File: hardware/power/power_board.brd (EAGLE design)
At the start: 75 x 64.5 mm, 6 parts, among them J1 FASTON_MALE_RA_BLADE, J2 FASTON_MALE_RA_BLADE, J3 12v, J4 5v, U1 PDQ30-Q24-S5-D, U2 PDQ30-Q24-S12-D

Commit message: Power updates
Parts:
- added J5, J6, J7, J8: XT30PW-F, timlib:XT30PW-F
- added R1: 100, rcl:R0603
- added U$10, U$9: 2, timlib:PWR163
- added U$11: PSMN1R0-40YSH, timlib:LFPAK56E
- moved J3 107.3 mm to (85.2, 81.6), turned to 90 degrees
- moved J4 94.3 mm to (85.2, 71.0), turned to 90 degrees
- moved U2 74.8 mm to (15.8, 77.0), turned to 0 degrees
- moved U1 45.6 mm to (15.8, 50.9), turned to 180 degrees
- moved J1 42.5 mm to (50.0, 57.3), turned to 180 degrees
- moved J2 23.8 mm to (50.0, 34.7), turned to 180 degrees
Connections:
- new net N$1: U$10.P$1, U$11.5
- net +24V: now also J5.P$2, J6.P$2, J7.P$2, J8.P$2
- net GND: now also J5.P$1, J6.P$1, J7.P$1, J8.P$1, U$11.1, U$11.2, U$11.3
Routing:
- removed copper zone on layer 16, net GND_5V
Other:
- board size 75 x 64.5 mm -> 92 x 92 mm

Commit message: Power board updates
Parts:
- added R2, R5: 2, timlib:PWR163
- added R4: 100, rcl:R0603
- added U$12: SMAJ12A, timlib:DO-214AC
- U$10: value 2 -> SMAJ12A; device timlib:PWR163 -> timlib:DO-214AC
- U$9: value 2 -> PSMN1R0-40YSH; device timlib:PWR163 -> timlib:LFPAK56E
- moved U$11 40.8 mm to (24.3, 33.9), turned to 270 degrees
- moved U$10 40.6 mm to (23.6, 16.5)
- moved R1 37.9 mm to (23.2, 24.0)
- moved U$9 8.64 mm to (15.6, 16.8), turned to 90 degrees
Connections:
- new net N$2: R1.1, U$11.4, U$12.C
- new net N$3: R5.P$2, U$9.5
- new net N$4: R4.1, U$10.C, U$9.4
- net GND: now also U$10.A, U$12.A, U$9.1, U$9.2, U$9.3
- net N$1: now also R2.P$2; no longer U$10.P$1
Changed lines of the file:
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@@
 <element name="U1" library="timlib" library_urn="urn:adsk.eagle:library:16152524" package="PDQ30-D" package3d_urn="urn:adsk.eagle:package:16187995/2" value="PDQ30-Q24-S5-D" x="15.75" y="50.85" smashed="yes" rot="R180"/>
 <element name="U2" library="timlib" library_urn="urn:adsk.eagle:library:16152524" package="PDQ30-D" package3d_urn="urn:adsk.eagle:package:16187995/2" value="PDQ30-Q24-S12-D" x="15.75" y="76.95" smashed="yes"/>
-<element name="J5" library="timlib" library_urn="urn:adsk.eagle:library:16152524" package="XT30PW-F" package3d_urn="urn:adsk.eagle:package:16203166/6" value="XT30PW-F" x="80.85" y="25.75" smashed="yes" rot="R270" grouprefs="EXTERNAL_PLUGS LEG_POWER"/>
-<element name="J6" library="timlib" library_urn="urn:adsk.eagle:library:16152524" package="XT30PW-F" package3d_urn="urn:adsk.eagle:package:16203166/6" value="XT30PW-F" x="80.85" y="39.5" smashed="yes" rot="R270" grouprefs="EXTERNAL_PLUGS LEG_POWER"/>
-<element name="J7" library="timlib" library_urn="urn:adsk.eagle:library:16152524" package="XT30PW-F" package3d_urn="urn:adsk.eagle:package:16203166/6" value="XT30PW-F" x="80.85" y="53.25" smashed="yes" rot="R270" grouprefs="EXTERNAL_PLUGS LEG_POWER"/>
-<element name="J8" library="timlib" library_urn="urn:adsk.eagle:library:16152524" package="XT30PW-F" package3d_urn="urn:adsk.eagle:package:16203166/6" value="XT30PW-F" x="80.85" y="12" smashed="yes" rot="R270" grouprefs="EXTERNAL_PLUGS LEG_POWER"/>
-<element name="U$9" library="timlib" library_urn="urn:adsk.eagle:library:16152524" package="PWR163" package3d_urn="urn:adsk.eagle:package:16220013/7" value="2" x="8.85" y="22.2" smashed="yes" rot="R180"/>
-<element name="U$10" library="timlib" library_urn="urn:adsk.eagle:library:16152524" package="PWR163" package3d_urn="urn:adsk.eagle:package:16220013/7" value="2" x="34.2" y="55.65" smashed="yes" rot="R270"/>
-<element name="U$11" library="timlib" library_urn="urn:adsk.eagle:library:16152524" package="LFPAK56E" package3d_urn="urn:adsk.eagle:package:16249927/3" value="PSMN1R0-40YSH" x="-2.7" y="3.3" smashed="yes"/>
-<element name="R1" library="rcl" library_urn="urn:adsk.eagle:library:334" package="R0603" package3d_urn="urn:adsk.eagle:package:23555/3" value="100" x="-3.6" y="-2.7" smashed="yes">
-<attribute name="NAME" x="-4.235" y="-2.065" size="1.27" layer="25"/>
-<attribute name="POPULARITY" value="77" x="-3.6" y="-2.7" size="1.778" layer="27" display="off"/>
-<attribute name="SPICEPREFIX" value="R" x="-3.6" y="-2.7" size="1.778" layer="27" display="off"/>
-<attribute name="VALUE" x="-4.235" y="-4.605" size="1.27" layer="27"/>
+<element name="J5" library="timlib" library_urn="urn:adsk.eagle:library:16152524" package="XT30PW-F" package3d_urn="urn:adsk.eagle:package:16203166/6" value="XT30PW-F" x="80.85" y="25.75" smashed="yes" rot="R270" grouprefs="LEG_POWER EXTERNAL_PLUGS"/>
+<element name="J6" library="timlib" library_urn="urn:adsk.eagle:library:16152524" package="XT30PW-F" package3d_urn="urn:adsk.eagle:package:16203166/6" value="XT30PW-F" x="80.85" y="39.5" smashed="yes" rot="R270" grouprefs="LEG_POWER EXTERNAL_PLUGS"/>
+<element name="J7" library="timlib" library_urn="urn:adsk.eagle:library:16152524" package="XT30PW-F" package3d_urn="urn:adsk.eagle:package:16203166/6" value="XT30PW-F" x="80.85" y="53.25" smashed="yes" rot="R270" grouprefs="LEG_POWER EXTERNAL_PLUGS"/>
+<element name="J8" library="timlib" library_urn="urn:adsk.eagle:library:16152524" package="XT30PW-F" package3d_urn="urn:adsk.eagle:package:16203166/6" value="XT30PW-F" x="80.85" y="12" smashed="yes" rot="R270" grouprefs="LEG_POWER EXTERNAL_PLUGS"/>
+<element name="U$11" library="timlib" library_urn="urn:adsk.eagle:library:16152524" package="LFPAK56E" package3d_urn="urn:adsk.eagle:package:16249927/3" value="PSMN1R0-40YSH" x="24.3" y="33.9" smashed="yes" rot="R270"/>
+<element name="R1" library="rcl" library_urn="urn:adsk.eagle:library:334" package="R0603" package3d_urn="urn:adsk.eagle:package:23555/3" value="100" x="23.25" y="24" smashed="yes">
+<attribute name="NAME" x="22.615" y="24.635" size="1.27" layer="25"/>
+<attribute name="POPULARITY" value="77" x="23.25" y="24" size="1.778" layer="27" display="off"/>
+<attribute name="SPICEPREFIX" value="R" x="23.25" y="24" size="1.778" layer="27" display="off"/>
+<attribute name="VALUE" x="22.615" y="22.095" size="1.27" layer="27"/>
 </element>
+<element name="U$12" library="timlib" library_urn="urn:adsk.eagle:library:16152524" package="DO-214AC" package3d_urn="urn:adsk.eagle:package:16356227/5" value="SMAJ12A" x="33.45" y="25.95" smashed="yes" rot="R90">
+<attribute name="NAME" x="31.545" y="23.41" size="1.27" layer="25" rot="R90"/>
+<attribute name="VALUE" x="36.625" y="23.41" size="1.27" layer="27" rot="R90"/>
+</element>
+<element name="R2" library="timlib" library_urn="urn:adsk.eagle:library:16152524" package="PWR163" package3d_urn="urn:adsk.eagle:package:16220013/7" value="2" x="34.95" y="42.6" smashed="yes" rot="R270"/>
+<element name="U$9" library="timlib" library_urn="urn:adsk.eagle:library:16152524" package="LFPAK56E" package3d_urn="urn:adsk.eagle:package:16249927/3" value="PSMN1R0-40YSH" x="15.6" y="16.8" smashed="yes" rot="R90"/>
+<element name="R4" library="rcl" library_urn="urn:adsk.eagle:library:334" package="R0603" package3d_urn="urn:adsk.eagle:package:23555/3" value="100" x="29.1" y="19.95" smashed="yes">
+<attribute name="NAME" x="28.465" y="20.585" size="1.27" layer="25"/>
+<attribute name="POPULARITY" value="77" x="24" y="41.7" size="1.778" layer="27" display="off"/>
+<attribute name="SPICEPREFIX" value="R" x="24" y="41.7" size="1.778" layer="27" display="off"/>
+<attribute name="VALUE" x="28.465" y="18.045" size="1.27" layer="27"/>
+</element>
+<element name="U$10" library="timlib" library_urn="urn:adsk.eagle:library:16152524" package="DO-214AC" package3d_urn="urn:adsk.eagle:package:16356227/5" value="SMAJ12A" x="23.55" y="16.5" smashed="yes" rot="R270">
+<attribute name="NAME" x="25.455" y="19.04" size="1.27" layer="25" rot="R270"/>
+<attribute name="VALUE" x="20.375" y="19.04" size="1.27" layer="27" rot="R270"/>
+</element>
+<element name="R5" library="timlib" library_urn="urn:adsk.eagle:library:16152524" package="PWR163" package3d_urn="urn:adsk.eagle:package:16220013/7" value="2" x="7.35" y="14.1" smashed="yes" rot="R180"/>
 </elements>
 <signals>
@@
 <contactref element="U$11" pad="1"/>
 <contactref element="U$11" pad="2"/>
+<contactref element="U$12" pad="A"/>
+<contactref element="U$9" pad="1"/>
+<contactref element="U$9" pad="2"/>
+<contactref element="U$9" pad="3"/>
+<contactref element="U$10" pad="A"/>
 <wire x1="75.85" y1="42" x2="75.85" y2="55.75" width="0" layer="19" extent="1-1"/>
 <wire x1="75.85" y1="28.25" x2="75.85" y2="42" width="0" layer="19" extent="1-1"/>
@@
 <wire x1="52.54" y1="34.7" x2="75.85" y2="28.25" width="0" layer="19" extent="1-1"/>
 <wire x1="47.46" y1="34.7" x2="52.54" y2="34.7" width="0" layer="19" extent="1-1"/>
-<wire x1="13.21" y1="40.69" x2="47.46" y2="34.7" width="0" layer="19" extent="1-1"/>
-<wire x1="-2.065" y1="0.575" x2="13.21" y2="40.69" width="0" layer="19" extent="1-1"/>
-<wire x1="-3.335" y1="0.575" x2="-2.065" y2="0.575" width="0" layer="19" extent="1-1"/>
-<wire x1="-4.605" y1="0.575" x2="-3.335" y2="0.575" width="0" layer="19" extent="1-1"/>
+<wire x1="21.575" y1="35.805" x2="47.46" y2="34.7" width="0" layer="19" extent="1-1"/>
+<wire x1="21.575" y1="34.535" x2="21.575" y2="35.805" width="0" layer="19" extent="1-1"/>
+<wire x1="21.575" y1="33.265" x2="21.575" y2="34.535" width="0" layer="19" extent="1-1"/>
+<wire x1="33.45" y1="27.975" x2="21.575" y2="33.265" width="0" layer="19" extent="1-1"/>
+<wire x1="13.21" y1="40.69" x2="21.575" y2="35.805" width="0" layer="19" extent="1-1"/>
 <wire x1="18.29" y1="87.11" x2="13.21" y2="40.69" width="0" layer="19" extent="1-1"/>
+<wire x1="23.55" y1="14.475" x2="33.45" y2="27.975" width="0" layer="19" extent="1-1"/>
+<wire x1="18.325" y1="14.895" x2="23.55" y2="14.475" width="0" layer="19" extent="1-1"/>
+<wire x1="18.325" y1="16.165" x2="18.325" y2="14.895" width="0" layer="19" extent="1-1"/>
+<wire x1="18.325" y1="17.435" x2="18.325" y2="16.165" width="0" layer="19" extent="1-1"/>
 </signal>
 <signal name="N$1">
-<contactref element="U$10" pad="P$1"/>
 <contactref element="U$11" pad="5"/>
-<wire x1="-2.7" y1="5.332" x2="32.295" y2="58.19" width="0" layer="19" extent="1-1"/>
+<contactref element="R2" pad="P$2"/>
+<wire x1="26.332" y1="33.9" x2="33.045" y2="40.06" width="0" layer="19" extent="1-1"/>
+</signal>
+<signal name="N$2">
+<contactref element="U$12" pad="C"/>
+<contactref element="U$11" pad="4"/>
+<contactref element="R1" pad="1"/>
+<wire x1="22.4" y1="24" x2="33.45" y2="23.925" width="0" layer="19" extent="1-1"/>
+<wire x1="21.575" y1="31.995" x2="22.4" y2="24" width="0" layer="19" extent="1-1"/>
+</signal>
+<signal name="N$3">
+<contactref element="U$9" pad="5"/>
+<contactref element="R5" pad="P$2"/>
+<wire x1="13.568" y1="16.8" x2="4.81" y2="16.005" width="0" layer="19" extent="1-1"/>
+</signal>
+<signal name="N$4">
+<contactref element="U$10" pad="C"/>
+<contactref element="U$9" pad="4"/>
+<contactref element="R4" pad="1"/>
+<wire x1="23.55" y1="18.525" x2="28.25" y2="19.95" width="0" layer="19" extent="1-1"/>
+<wire x1="18.325" y1="18.705" x2="23.55" y2="18.525" width="0" layer="19" extent="1-1"/>
 </signal>
 </signals>

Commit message: Missing some caps
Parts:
- added C1, C2, C3, C4, C5, C6, C7: 220uf, timlib:C_ELEC_8X11_5
- added IC1, IC2: LM321MF, linear:SOT23-5
- added R10, R15, R17, R19, R7, R9: 100k\, rcl:R0603
- added R11: 4.7k, rcl:R0603
- added R12: 2, timlib:PWR163
- added R13, R3: 873.1k, rcl:R0603
- added R14: 100k, rcl:R0603
- added R16, R18, R6, R8: 400k, rcl:R0603
- added U$1, U$2, U$3, U$6: PSMN1R0-40YSH, timlib:LFPAK56E
- added U$4, U$7, U$8: SMAJ12A, timlib:DO-214AC
- added U$5: LP2951ACMM/NOPB, timlib:LP2591
- R1: value 100 -> 4.7k
- R4: value 100 -> 100k
- R5: value 2 -> 100k\; device timlib:PWR163 -> rcl:R0603
- U$9: value PSMN1R0-40YSH -> LP2951ACMM/NOPB; device timlib:LFPAK56E -> timlib:LP2591
- moved U$9 48.7 mm to (64.2, 13.5), turned to 0 degrees
- moved R5 47.2 mm to (53.4, 24.3), turned to 0 degrees
- moved U$10 40.9 mm to (3.00, -18.9), turned to 0 degrees
- moved R2 40.4 mm to (7.05, 13.3), turned to 180 degrees
- moved R4 27.4 mm to (54.8, 10.3)
- moved R1 24.3 mm to (39.9, 41.7)
- moved U$12 19.0 mm to (45.1, 41.0), turned to 0 degrees
- moved U$11 11.0 mm to (33.1, 40.4), turned to 90 degrees
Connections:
- net GND_12V renamed -12VOUT
- net GND_5V renamed -5VOUT
- net ISO_+12V renamed +12VOUT
- net ISO_+5V renamed +5VOUT
- removed net +24V: J1.P$1, J1.P$2, J5.P$2, J6.P$2, J7.P$2, J8.P$2, U1.P$1, U2.P$1
- new net BATT_+24V: C1.1, C2.1, C3.1, C4.1, C5.1, C6.1, C7.1, J1.P$1, J1.P$2, J5.P$2, J6.P$2, J7.P$2, J8.P$2, U$5.8, U$9.8, U1.P$1, U2.P$1
- new net BATT_GND: IC1.2, IC2.2, J2.P$1, J2.P$2, R14.1, R16.1, R18.1, R4.1, R6.1, R8.1, U$1.1, U$1.2, U$1.3, U$10.A, U$11.1, U$11.2, U$11.3, U$12.A, U$2.1, U$2.2, U$2.3, U$3.1, U$3.2, U$3.3, U$4.A, U$5.3, U$5.4, U$8.A, U$9.3, U$9.4
- new net ISO_12V: IC2.5, R11.2, R13.2, R15.2, R17.2, U$5.1
- new net ISO_GND: R12.P$2, U$6.5, U1.P$2, U2.P$2
- new net LEG_12V: IC1.5, R1.2, R3.2, R5.2, R7.2, U$9.1
- new net LEG_GND: C1.2, C2.2, C3.2, C4.2, C5.2, C6.2, C7.2, J5.P$1, J6.P$1, J7.P$1, J8.P$1, R2.P$1, U$1.5, U$2.5
- new net N$10: R13.1, R14.2, U$5.7
- new net N$11: R12.P$1, U$3.5
- new net N$12: IC2.3, R15.1, R16.2
- new net N$13: IC2.1, R17.1, R18.2
- new net N$14: IC2.4, R19.2
- new net N$15: R19.1, U$6.4, U$7.C
- new net N$5: IC1.1, R7.1, R8.2
- new net N$6: IC1.4, R10.2, R9.2
- new net N$7: R11.1, U$3.4, U$4.C
- new net N$8: R9.1, U$1.4, U$8.C
- new net N$9: R10.1, U$10.C, U$2.4
- net GND: now also U$6.1, U$6.2, U$6.3, U$7.A; no longer J2.P$1, J2.P$2, J5.P$1, J6.P$1, J7.P$1, J8.P$1, U$10.A, U$11.1, U$11.2, U$11.3, U$12.A, U$9.1, U$9.2, U$9.3, U1.P$2, U2.P$2
- net N$3: now also R3.1, R4.2, U$9.7; no longer R5.P$2, U$9.5
- net N$4: now also IC1.3, R5.1, R6.2; no longer R4.1, U$10.C, U$9.4

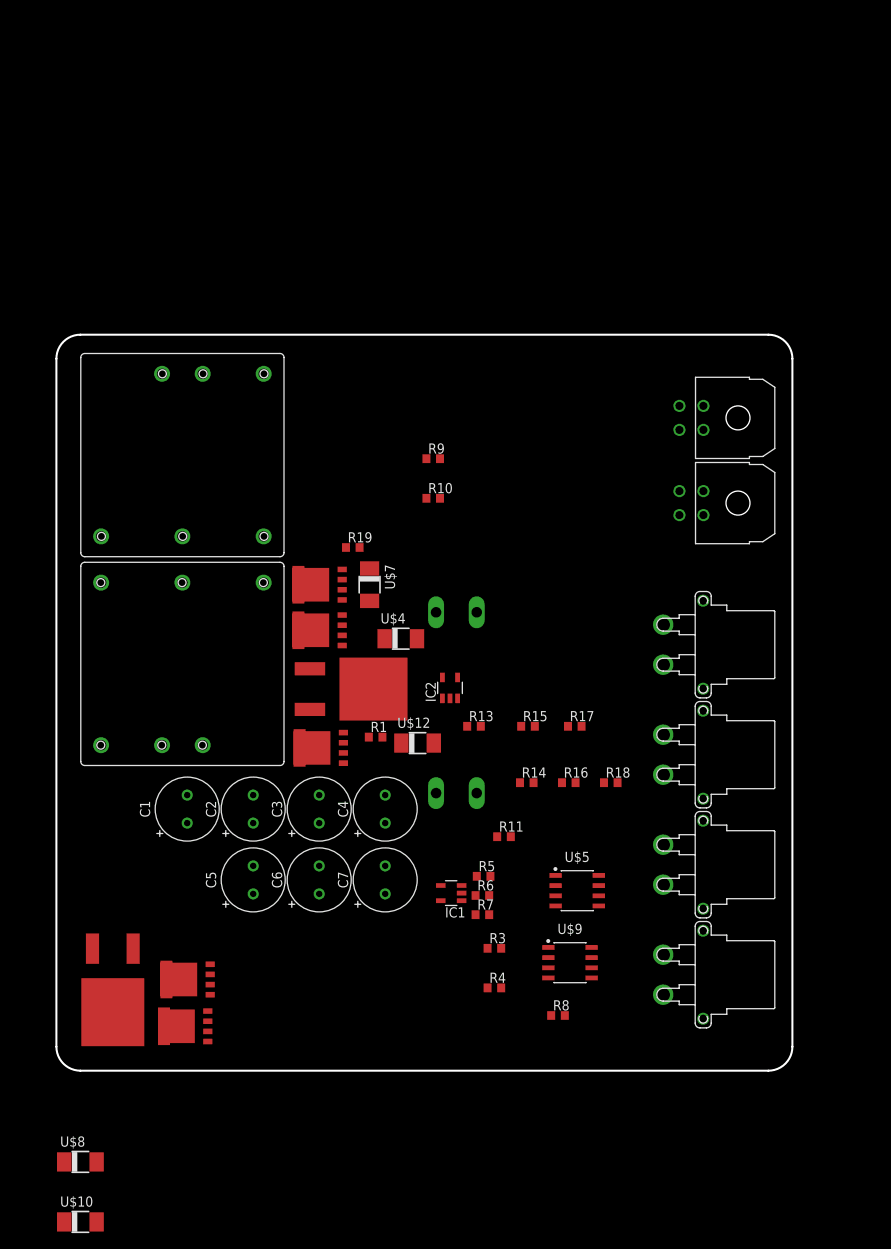
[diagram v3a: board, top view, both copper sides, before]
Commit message: More caps
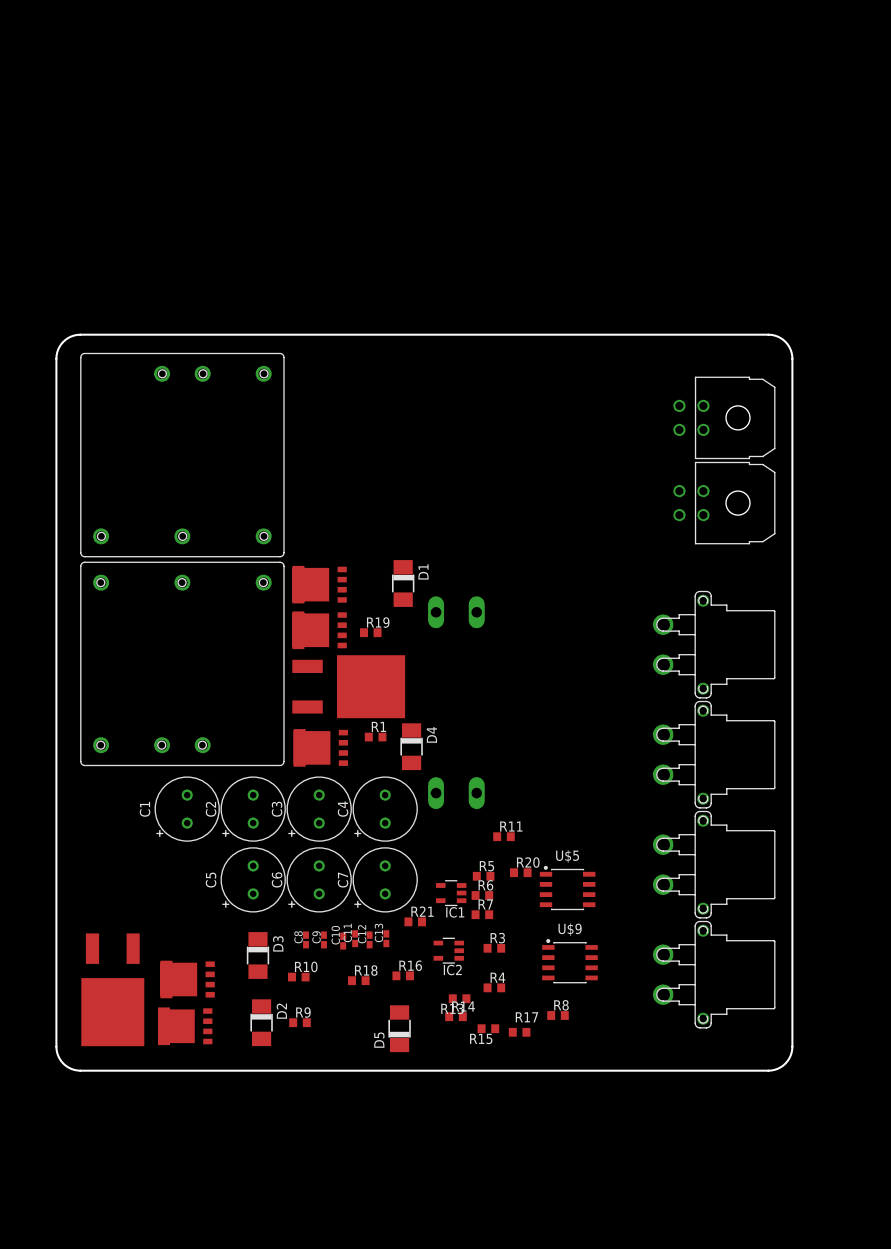
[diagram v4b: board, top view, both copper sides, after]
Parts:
- removed U$10, U$12, U$4, U$7, U$8: SMAJ12A, timlib:DO-214AC
- added C10, C11, C8, C9: 2.2uF, timlib:C0402K
- added C12, C13: 300nF, timlib:C0402K
- added D1, D2, D3, D4, D5: SMAJ12A, timlib:DO-214AC
- added R20, R21: 0.5, rcl:R0603
- R18, R8: value 400k -> 500k
- moved R9 72.4 mm to (30.4, 6.00)
- moved R10 62.2 mm to (30.3, 11.7)
- moved R18 40.1 mm to (37.8, 11.2)
- moved R17 38.9 mm to (57.9, 4.80)
- moved R15 38.1 mm to (54.0, 5.25), turned to 180 degrees
- moved R13 34.1 mm to (50.4, 9.00), turned to 180 degrees
- moved IC2 32.9 mm to (49.0, 15.0), turned to 90 degrees
- moved R16 31.8 mm to (43.4, 11.8)
- moved R14 30.6 mm to (50.0, 6.75)
- moved R19 10.9 mm to (39.3, 54.8)
- moved U$5 1.21 mm to (63.9, 22.6)
- moved R12 0.42 mm to (33.3, 48.0)
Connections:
- new net BATT_+24V1: C10.1
- new net N$16: C9.1, R20.1
- new net N$17: C11.1, R21.1
- net BATT_+24V: now also C8.1
- net BATT_GND: now also D2.A, D3.A, D4.A, D5.A; no longer U$10.A, U$12.A, U$4.A, U$8.A
- net GND: now also C10.2, C11.2, C12.2, C13.2, C8.2, C9.2, D1.A; no longer U$7.A
- net ISO_12V: now also R20.2
- net LEG_12V: now also R21.2
- net N$13: now also C13.1
- net N$15: now also D1.C; no longer U$7.C
- net N$2: now also D4.C; no longer U$12.C
- net N$5: now also C12.1
- net N$7: now also D5.C; no longer U$4.C
- net N$8: now also D3.C; no longer U$8.C
- net N$9: now also D2.C; no longer U$10.C

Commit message: More updates to power board
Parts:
- added U$26, U$27: 2-PIN, timlib:M80-8420242
- added U$4: CDBB5100-HF, timlib:DO-214AA
- R10, R19, R9: value 100k\ -> 4.7k
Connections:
- net -12VOUT renamed 12V_GND
- net -5VOUT renamed 5V_GND
- removed net BATT_+24V: C1.1, C2.1, C3.1, C4.1, C5.1, C6.1, C7.1, C8.1, J1.P$1, J1.P$2, J5.P$2, J6.P$2, J7.P$2, J8.P$2, U$5.8, U$9.8, U1.P$1, U2.P$1
- removed net BATT_+24V1: C10.1
- removed net GND: C10.2, C11.2, C12.2, C13.2, C8.2, C9.2, D1.A, U$6.1, U$6.2, U$6.3
- new net +24V: C1.1, C2.1, C3.1, C4.1, C5.1, C6.1, C7.1, J1.P$1, J1.P$2, J5.P$2, J6.P$2, J7.P$2, J8.P$2, U$26.1, U$27.1, U$4.C, U1.P$1, U2.P$1
- new net N$18: C8.1, U$26.2, U$5.8
- new net N$19: C10.1, U$27.2, U$9.8
- net BATT_GND: now also C10.2, C11.2, C12.2, C13.2, C8.2, C9.2, D1.A, U$6.1, U$6.2, U$6.3
- net LEG_GND: now also U$4.A
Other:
- board text added: "+"
- board text added: "-"

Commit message: part moving
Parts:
- C10, C11, C12, C13, C8, C9: device timlib:C0402K -> timlib:C0603
- moved R2 97.3 mm to (39.5, 105.2)
- moved R1 94.2 mm to (74.5, 129.3)
- moved R3 94.2 mm to (89.4, 102.9)
- moved R4 94.2 mm to (89.4, 98.0)
- moved R5 94.2 mm to (88.0, 111.9)
- moved U$1 94.2 mm to (50.9, 93.2)
- moved C10 94.2 mm to (70.5, 103.8)
- moved C11 94.2 mm to (72.0, 104.1)
- moved C12 94.2 mm to (73.8, 104.0)
- moved D2 94.2 mm to (60.3, 93.6)
- moved D4 94.2 mm to (79.0, 128.1)
- moved IC1 94.2 mm to (84.0, 109.8)
- moved R10 94.2 mm to (65.0, 99.3)
- moved R21 94.2 mm to (79.5, 106.2)
- moved R6 94.2 mm to (87.9, 109.5)
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
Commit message: Updates to power board
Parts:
- J1, J2: value FASTON_MALE_RA_BLADE -> FASTON1289_ST; device timlib:FASTON_MALE_RA_BLADE -> timlib:FASTON_1289-ST
- moved D4 98.5 mm to (42.3, 36.8)
- moved U$11 97.7 mm to (32.9, 36.8)
- moved R1 97.1 mm to (45.3, 36.8), turned to 270 degrees
- moved IC1 92.5 mm to (48.4, 24.4), turned to 270 degrees
- moved R6 92.1 mm to (52.6, 24.4), turned to 90 degrees
- moved U$27 91.1 mm to (63.9, 10.7)
- moved R5 90.5 mm to (52.6, 28.6), turned to 90 degrees
- moved R7 83.4 mm to (59.7, 28.6), turned to 90 degrees
- moved U$9 82.7 mm to (65.7, 25.4)
- moved R3 81.3 mm to (56.2, 28.6), turned to 90 degrees
- moved R4 80.7 mm to (56.1, 24.4), turned to 90 degrees
- moved R8 79.5 mm to (59.7, 24.4), turned to 90 degrees
- moved C12 79.5 mm to (48.4, 28.6), turned to 180 degrees
- moved R21 78.9 mm to (62.6, 29.1), turned to 180 degrees
- moved C11 75.3 mm to (65.7, 29.1), turned to 0 degrees
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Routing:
- net ISO_12V: track 0.00 -> 46.9 mm
- net N$6: track 0.00 -> 42.9 mm
- net N$19: track 0.00 -> 27.9 mm
- net LEG_12V: track 0.00 -> 27.5 mm, vias 0 -> 2
- net N$14: track 0.00 -> 22.5 mm
- net N$18: track 0.00 -> 22.1 mm
- net N$3: track 0.00 -> 19.3 mm
- net N$13: track 0.00 -> 19.1 mm, vias 0 -> 3
- net N$5: track 0.00 -> 18.8 mm, vias 0 -> 2
- net N$10: track 0.00 -> 15.0 mm, vias 0 -> 2
- net N$12: track 0.00 -> 14.2 mm, vias 0 -> 2
- net N$8: track 0.00 -> 11.6 mm
- net N$9: track 0.00 -> 10.3 mm
- net N$2: track 0.00 -> 10.3 mm
- net N$7: track 0.00 -> 9.12 mm
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- added copper zone on layer 1, net BATT_GND
- added copper zone on layer 1, net ISO_GND
- added copper zone on layer 1, net N$1
- added copper zone on layer 1, net N$11
